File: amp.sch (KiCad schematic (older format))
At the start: 25 parts, among them Q2 MMBF170, Q3 IRF510, Q4 IRF510, T1 8:8, T2 8:8, T3 2:3

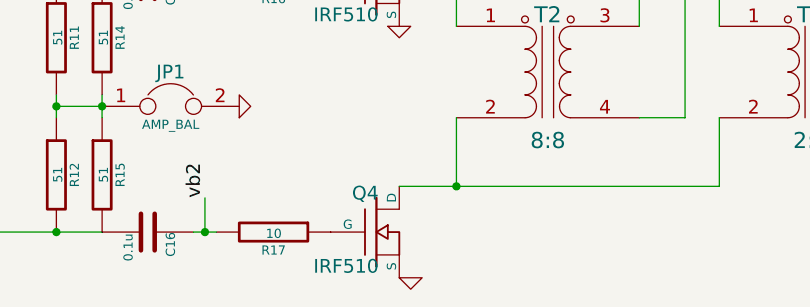
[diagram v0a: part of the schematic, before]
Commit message: All layed out
Several net errors fixed, and some mcu pins reassigned for better layout.
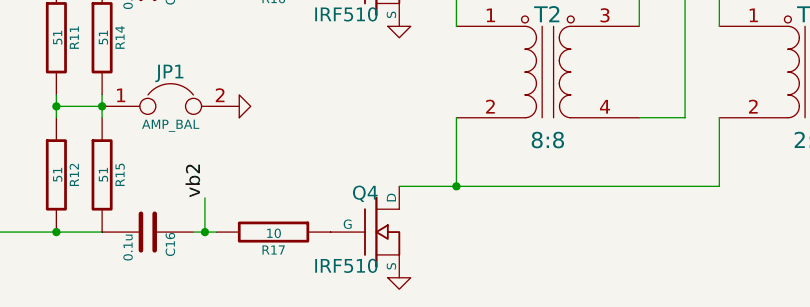
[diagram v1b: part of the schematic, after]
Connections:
- net GND: now also Q4.S
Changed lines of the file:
@@
 L GND #PWR047
 U 1 1 5470F610
-P 7150 5600
-F 0 "#PWR047" H 7150 5600 30  0001 C CNN
-F 1 "GND" H 7150 5530 30  0001 C CNN
-F 2 "" H 7150 5600 60  0000 C CNN
-F 3 "" H 7150 5600 60  0000 C CNN
-	1    7150 5600
+P 7100 5600
+F 0 "#PWR047" H 7100 5600 30  0001 C CNN
+F 1 "GND" H 7100 5530 30  0001 C CNN
+F 2 "" H 7100 5600 60  0000 C CNN
+F 3 "" H 7100 5600 60  0000 C CNN
+	1    7100 5600
 	1    0    0    -1
 $EndComp

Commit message: Schematic changes to go with #3 (extending sot23 pads)
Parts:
- Q2: footprint nu9j-footprints:sot23-DGS -> nu9j-footprints:SOT-23-DGS_HandSoldering
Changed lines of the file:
@@
 F 0 "Q2" H 4660 3670 60  0000 R CNN
 F 1 "MMBF170" H 4660 3350 60  0000 R CNN
-F 2 "nu9j-footprints:sot23-DGS" H 4650 3500 60  0001 C CNN
+F 2 "nu9j-footprints:SOT-23-DGS_HandSoldering" H 4650 3500 60  0001 C CNN
 F 3 "" H 4650 3500 60  0000 C CNN
 	1    4650 3500

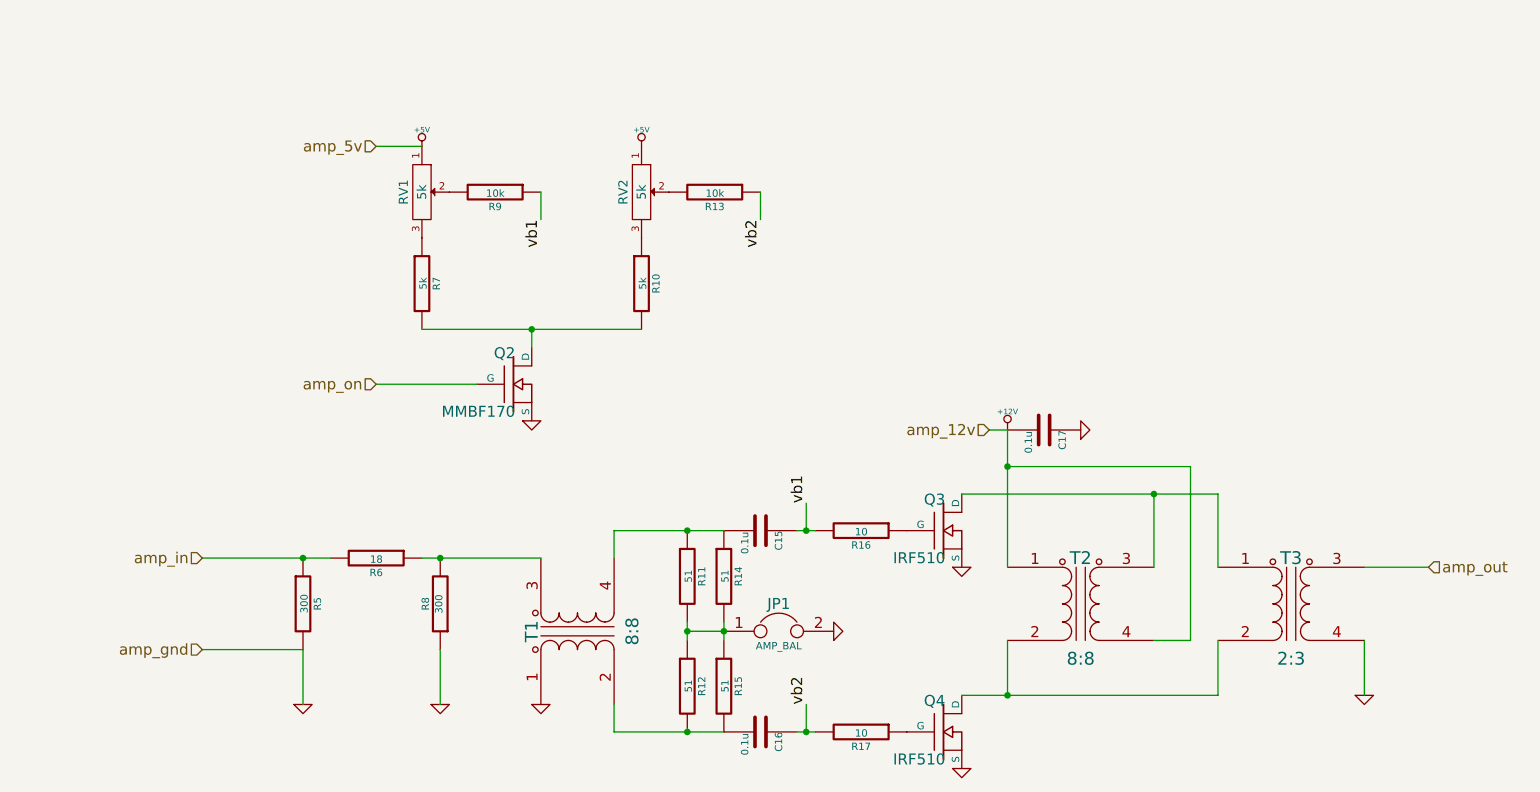
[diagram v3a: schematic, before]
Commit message: Fixes #9: gate bias broken
Replaces Q2 with LTV-356T opto-coupler between 5V and bias rail
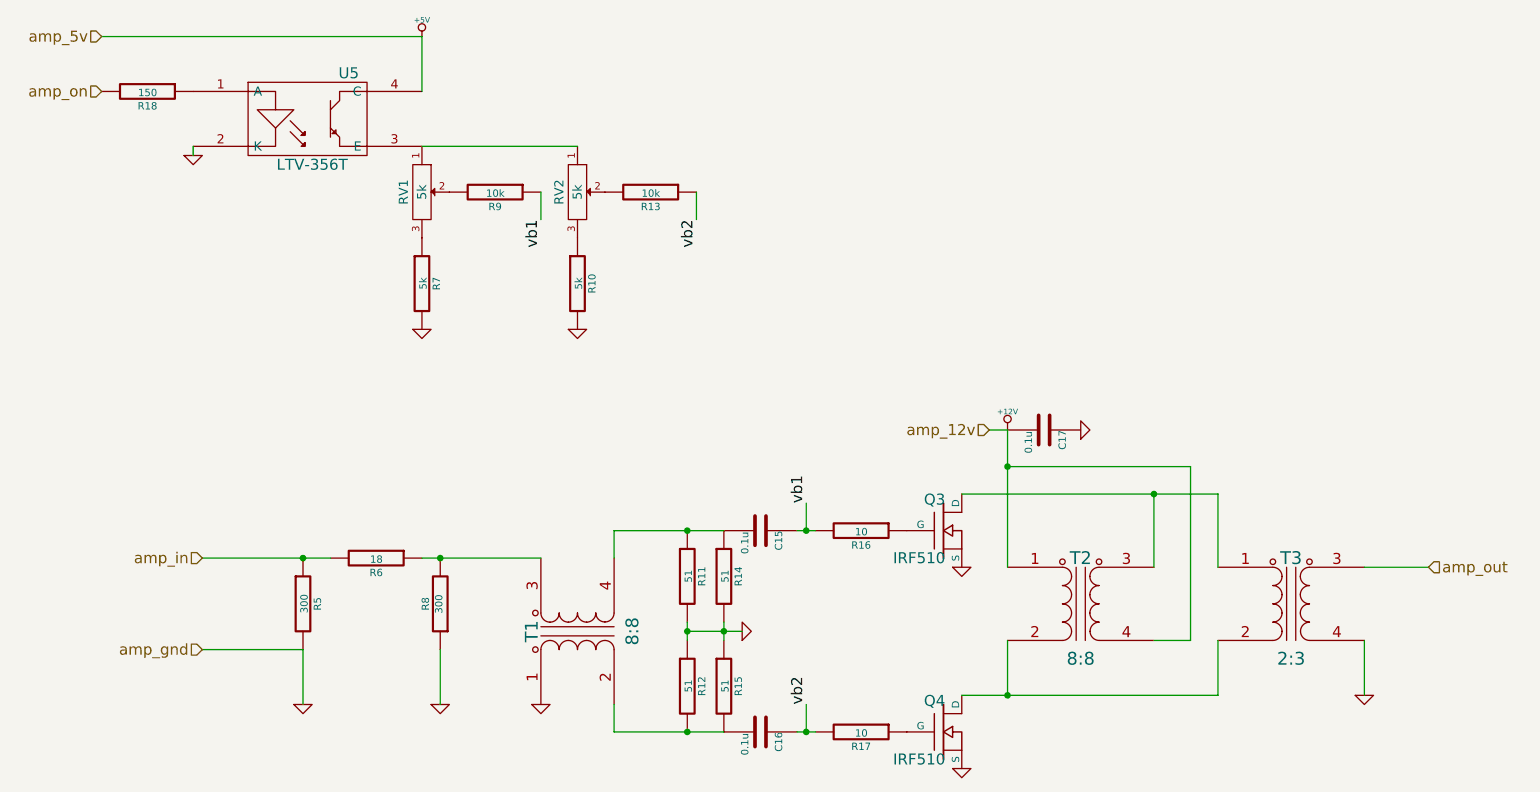
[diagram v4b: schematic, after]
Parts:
- removed JP1: AMP_BAL, Pin_Headers:Pin_Header_Straight_1x02, symbol JUMPER
- removed Q2: MMBF170, nu9j-footprints:SOT-23-DGS_HandSoldering, symbol MOSFET_N
- added R18: 150, Resistors_SMD:R_1206_HandSoldering, symbol R
- added U5: LTV-356T, Opto-Devices:Optocoupler_SMD_HandSoldering_KPC357_LTV35x_PC357_SingleChannel, symbol OPTO-TRANSISTOR4
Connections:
- net +5V: now also U5.4 (C); no longer RV1.1, RV2.1
- net GND: now also R10.2, R11.2, R12.1, R14.2, R15.1, R7.2, U5.2 (K)
- net amp_on: now also R18.2
- new net: RV1.1, RV2.1, U5.3 (E)
- new net: R18.1, U5.1 (A)
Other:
- moved on the sheet: R10, R13, RV2
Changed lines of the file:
@@
 L POT RV2
 U 1 1 5470F7B3
-P 5350 2450
-F 0 "RV2" H 5350 2350 50  0000 C CNN
-F 1 "5k" H 5350 2450 50  0000 C CNN
-F 2 "nu9j-footprints:Potentiometer_Trimmer_Piher_PT10_H01" H 5350 2450 60  0001 C CNN
-F 3 "" H 5350 2450 60  0000 C CNN
-	1    5350 2450
+P 5000 2450
+F 0 "RV2" H 5000 2350 50  0000 C CNN
+F 1 "5k" H 5000 2450 50  0000 C CNN
+F 2 "nu9j-footprints:Potentiometer_Trimmer_Piher_PT10_H01" H 5000 2450 60  0001 C CNN
+F 3 "" H 5000 2450 60  0000 C CNN
+	1    5000 2450
 	0    1    1    0
 $EndComp
@@
 L R R10
 U 1 1 5470F7D4
-P 5350 2950
-F 0 "R10" V 5430 2950 40  0000 C CNN
-F 1 "5k" V 5357 2951 40  0000 C CNN
-F 2 "Resistors_SMD:R_1206_HandSoldering" V 5280 2950 30  0001 C CNN
-F 3 "" H 5350 2950 30  0000 C CNN
-	1    5350 2950
+P 5000 2950
+F 0 "R10" V 5080 2950 40  0000 C CNN
+F 1 "5k" V 5007 2951 40  0000 C CNN
+F 2 "Resistors_SMD:R_1206_HandSoldering" V 4930 2950 30  0001 C CNN
+F 3 "" H 5000 2950 30  0000 C CNN
+	1    5000 2950
 	1    0    0    -1
 $EndComp
@@
 L R R13
 U 1 1 5470F80E
-P 5750 2450
-F 0 "R13" V 5830 2450 40  0000 C CNN
-F 1 "10k" V 5757 2451 40  0000 C CNN
-F 2 "Resistors_SMD:R_1206_HandSoldering" V 5680 2450 30  0001 C CNN
-F 3 "" H 5750 2450 30  0000 C CNN
-	1    5750 2450
+P 5400 2450
+F 0 "R13" V 5480 2450 40  0000 C CNN
+F 1 "10k" V 5407 2451 40  0000 C CNN
+F 2 "Resistors_SMD:R_1206_HandSoldering" V 5330 2450 30  0001 C CNN
+F 3 "" H 5400 2450 30  0000 C CNN
+	1    5400 2450
 	0    1    1    0
 $EndComp
@@
 L +5V #PWR049
 U 1 1 5470F81B
-P 4150 2200
-F 0 "#PWR049" H 4150 2290 20  0001 C CNN
-F 1 "+5V" H 4150 2290 30  0000 C CNN
-F 2 "" H 4150 2200 60  0000 C CNN
-F 3 "" H 4150 2200 60  0000 C CNN
-	1    4150 2200
+P 4150 1600
+F 0 "#PWR049" H 4150 1690 20  0001 C CNN
+F 1 "+5V" H 4150 1690 30  0000 C CNN
+F 2 "" H 4150 1600 60  0000 C CNN
+F 3 "" H 4150 1600 60  0000 C CNN
+	1    4150 1600
 	1    0    0    -1
 $EndComp
@@
 L GND #PWR050
 U 1 1 5470F84C
-P 4750 3700
-F 0 "#PWR050" H 4750 3700 30  0001 C CNN
-F 1 "GND" H 4750 3630 30  0001 C CNN
-F 2 "" H 4750 3700 60  0000 C CNN
-F 3 "" H 4750 3700 60  0000 C CNN
-	1    4750 3700
+P 2900 2250
+F 0 "#PWR050" H 2900 2250 30  0001 C CNN
+F 1 "GND" H 2900 2180 30  0001 C CNN
+F 2 "" H 2900 2250 60  0000 C CNN
+F 3 "" H 2900 2250 60  0000 C CNN
+	1    2900 2250
 	1    0    0    -1
 $EndComp
@@
 vb1
 Wire Wire Line
-	6000 2450 6000 2600
-Text Label 6000 2600 3    60   ~ 0
+	5650 2450 5650 2600
+Text Label 5650 2600 3    60   ~ 0
 vb2
 Wire Wire Line
@@
 L GND #PWR053
 U 1 1 5470FB98
-P 6400 4850
-F 0 "#PWR053" H 6400 4850 30  0001 C CNN
-F 1 "GND" H 6400 4780 30  0001 C CNN
-F 2 "" H 6400 4850 60  0000 C CNN
-F 3 "" H 6400 4850 60  0000 C CNN
-	1    6400 4850
+P 5900 4850
+F 0 "#PWR053" H 5900 4850 30  0001 C CNN
+F 1 "GND" H 5900 4780 30  0001 C CNN
+F 2 "" H 5900 4850 60  0000 C CNN
+F 3 "" H 5900 4850 60  0000 C CNN
+	1    5900 4850
 	0    -1   -1   0
 $EndComp
 Wire Wire Line
-	5600 4850 5800 4850
+	5600 4850 5900 4850
 Connection ~ 5800 4850
 Connection ~ 5600 4850
-$Comp
-L JUMPER JP1
-U 1 1 5470FBEE
-P 6100 4850
-F 0 "JP1" H 6100 5000 60  0000 C CNN
-F 1 "AMP_BAL" H 6100 4770 40  0000 C CNN
-F 2 "Pin_Headers:Pin_Header_Straight_1x02" H 6100 4850 60  0001 C CNN
-F 3 "" H 6100 4850 60  0000 C CNN
-	1    6100 4850
-	1    0    0    -1
-$EndComp
-$Comp
-L MOSFET_N Q2
-U 1 1 5470FC2F
-P 4650 3500
-F 0 "Q2" H 4660 3670 60  0000 R CNN
-F 1 "MMBF170" H 4660 3350 60  0000 R CNN
-F 2 "nu9j-footprints:SOT-23-DGS_HandSoldering" H 4650 3500 60  0001 C CNN
-F 3 "" H 4650 3500 60  0000 C CNN
-	1    4650 3500
-	1    0    0    -1
-$EndComp
-Wire Wire Line
-	4150 3200 5350 3200
-Wire Wire Line
-	4750 3200 4750 3300
-Connection ~ 4750 3200
-$Comp
-L +5V #PWR054
-U 1 1 5470FCA2
-P 5350 2200
-F 0 "#PWR054" H 5350 2290 20  0001 C CNN
-F 1 "+5V" H 5350 2290 30  0000 C CNN
-F 2 "" H 5350 2200 60  0000 C CNN
-F 3 "" H 5350 2200 60  0000 C CNN
-	1    5350 2200
-	1    0    0    -1
-$EndComp
-Wire Wire Line
-	4450 3500 3900 3500
-Text HLabel 3900 3500 0    60   Input ~ 0
+Text HLabel 2400 1900 0    60   Input ~ 0
 amp_on
 Wire Wire Line
@@
 Wire Wire Line
 	7350 3750 7250 3750
-Wire Wire Line
-	4150 2200 3900 2200
-Text HLabel 3900 2200 0    60   Input ~ 0
+Text HLabel 2400 1600 0    60   Input ~ 0
 amp_5v
 Text HLabel 7250 3750 0    60   Input ~ 0
 amp_12v
+$Comp
+L OPTO-TRANSISTOR4 U5
+U 1 1 5596F157
+P 3550 2050
+F 0 "U5" H 3750 2300 60  0000 C CNN
+F 1 "LTV-356T" H 3550 1800 60  0000 C CNN
+F 2 "Opto-Devices:Optocoupler_SMD_HandSoldering_KPC357_LTV35x_PC357_SingleChannel" H 3550 2050 60  0001 C CNN
+F 3 "" H 3550 2050 60  0000 C CNN
+	1    3550 2050
+	1    0    0    -1
+$EndComp
+Wire Wire Line
+	2900 2200 2900 2250
+Wire Wire Line
+	4150 1900 4150 1600
+$Comp
+L GND #PWR055
+U 1 1 5596F601
+P 4150 3200
+F 0 "#PWR055" H 4150 3200 30  0001 C CNN
+F 1 "GND" H 4150 3130 30  0001 C CNN
+F 2 "" H 4150 3200 60  0000 C CNN
+F 3 "" H 4150 3200 60  0000 C CNN
+	1    4150 3200
+	1    0    0    -1
+$EndComp
+$Comp
+L GND #PWR056
+U 1 1 5596F624
+P 5000 3200
+F 0 "#PWR056" H 5000 3200 30  0001 C CNN
+F 1 "GND" H 5000 3130 30  0001 C CNN
+F 2 "" H 5000 3200 60  0000 C CNN
+F 3 "" H 5000 3200 60  0000 C CNN
+	1    5000 3200
+	1    0    0    -1
+$EndComp
+$Comp
+L R R18
+U 1 1 55970003
+P 2650 1900
+F 0 "R18" V 2730 1900 40  0000 C CNN
+F 1 "150" V 2657 1901 40  0000 C CNN
+F 2 "Resistors_SMD:R_1206_HandSoldering" V 2580 1900 30  0001 C CNN
+F 3 "" H 2650 1900 30  0000 C CNN
+	1    2650 1900
+	0    1    1    0
+$EndComp
+Wire Wire Line
+	4150 1600 2400 1600
+Wire Wire Line
+	4150 2200 5000 2200
 $EndSCHEMATC

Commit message: Fixes #8: transistor placement
Also, this is a major board layout change

- Added more 12V filtering caps
- Placed fuse in front of filtering caps
- Changed IRF510 footprints to horizontal lower side w/ mounting hole
- Expanded layout to fill new board size
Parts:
- Q3, Q4: footprint Transistors_TO-220:TO-220_FET-GDS_Vertical_LargePads -> Transistors_TO-220:TO-220_FET-GDS_Horizontal_MountedFromLS_LargePads
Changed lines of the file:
@@
 F 0 "Q3" H 7010 4470 60  0000 R CNN
 F 1 "IRF510" H 7010 4150 60  0000 R CNN
-F 2 "Transistors_TO-220:TO-220_FET-GDS_Vertical_LargePads" H 7000 4300 60  0001 C CNN
+F 2 "Transistors_TO-220:TO-220_FET-GDS_Horizontal_MountedFromLS_LargePads" H 7000 4300 60  0001 C CNN
 F 3 "" H 7000 4300 60  0000 C CNN
 	1    7000 4300
@@
 F 0 "Q4" H 7010 5570 60  0000 R CNN
 F 1 "IRF510" H 7010 5250 60  0000 R CNN
-F 2 "Transistors_TO-220:TO-220_FET-GDS_Vertical_LargePads" H 7000 5400 60  0001 C CNN
+F 2 "Transistors_TO-220:TO-220_FET-GDS_Horizontal_MountedFromLS_LargePads" H 7000 5400 60  0001 C CNN
 F 3 "" H 7000 5400 60  0000 C CNN
 	1    7000 5400
@@
 	2950 4450 3650 4450
 $Comp
-L GND #PWR043
+L GND #PWR048
 U 1 1 5470F4C6
 P 4800 5250
-F 0 "#PWR043" H 4800 5250 30  0001 C CNN
+F 0 "#PWR048" H 4800 5250 30  0001 C CNN
 F 1 "GND" H 4800 5180 30  0001 C CNN
 F 2 "" H 4800 5250 60  0000 C CNN
@@
 $EndComp
 $Comp
-L GND #PWR044
+L GND #PWR049
 U 1 1 5470F4DA
 P 4250 5250
-F 0 "#PWR044" H 4250 5250 30  0001 C CNN
+F 0 "#PWR049" H 4250 5250 30  0001 C CNN
 F 1 "GND" H 4250 5180 30  0001 C CNN
 F 2 "" H 4250 5250 60  0000 C CNN
@@
 $EndComp
 $Comp
-L GND #PWR045
+L GND #PWR050
 U 1 1 5470F4EE
 P 3500 5250
-F 0 "#PWR045" H 3500 5250 30  0001 C CNN
+F 0 "#PWR050" H 3500 5250 30  0001 C CNN
 F 1 "GND" H 3500 5180 30  0001 C CNN
 F 2 "" H 3500 5250 60  0000 C CNN
@@
 Connection ~ 7350 3950
 $Comp
-L GND #PWR046
+L GND #PWR051
 U 1 1 5470F5FC
 P 7100 4500
-F 0 "#PWR046" H 7100 4500 30  0001 C CNN
+F 0 "#PWR051" H 7100 4500 30  0001 C CNN
 F 1 "GND" H 7100 4430 30  0001 C CNN
 F 2 "" H 7100 4500 60  0000 C CNN
@@
 $EndComp
 $Comp
-L GND #PWR047
+L GND #PWR052
 U 1 1 5470F610
 P 7100 5600
-F 0 "#PWR047" H 7100 5600 30  0001 C CNN
+F 0 "#PWR052" H 7100 5600 30  0001 C CNN
 F 1 "GND" H 7100 5530 30  0001 C CNN
 F 2 "" H 7100 5600 60  0000 C CNN
@@
 amp_in
 $Comp
-L GND #PWR048
+L GND #PWR053
 U 1 1 5470F625
 P 9300 5200
-F 0 "#PWR048" H 9300 5200 30  0001 C CNN
+F 0 "#PWR053" H 9300 5200 30  0001 C CNN
 F 1 "GND" H 9300 5130 30  0001 C CNN
 F 2 "" H 9300 5200 60  0000 C CNN
@@
 $EndComp
 $Comp
-L +5V #PWR049
+L +5V #PWR054
 U 1 1 5470F81B
 P 4150 1600
-F 0 "#PWR049" H 4150 1690 20  0001 C CNN
+F 0 "#PWR054" H 4150 1690 20  0001 C CNN
 F 1 "+5V" H 4150 1690 30  0000 C CNN
 F 2 "" H 4150 1600 60  0000 C CNN
@@
 $EndComp
 $Comp
-L GND #PWR050
+L GND #PWR055
 U 1 1 5470F84C
 P 2900 2250
-F 0 "#PWR050" H 2900 2250 30  0001 C CNN
+F 0 "#PWR055" H 2900 2250 30  0001 C CNN
 F 1 "GND" H 2900 2180 30  0001 C CNN
 F 2 "" H 2900 2250 60  0000 C CNN
@@
 vb2
 $Comp
-L +12V #PWR051
+L +12V #PWR056
 U 1 1 5470F9E0
 P 7350 3750
-F 0 "#PWR051" H 7350 3700 20  0001 C CNN
+F 0 "#PWR056" H 7350 3700 20  0001 C CNN
 F 1 "+12V" H 7350 3850 30  0000 C CNN
 F 2 "" H 7350 3750 60  0000 C CNN
@@
 $EndComp
 $Comp
-L GND #PWR052
+L GND #PWR057
 U 1 1 5470FA0D
 P 7750 3750
-F 0 "#PWR052" H 7750 3750 30  0001 C CNN
+F 0 "#PWR057" H 7750 3750 30  0001 C CNN
 F 1 "GND" H 7750 3680 30  0001 C CNN
 F 2 "" H 7750 3750 60  0000 C CNN
@@
 $EndComp
 $Comp
-L GND #PWR053
+L GND #PWR058
 U 1 1 5470FB98
 P 5900 4850
-F 0 "#PWR053" H 5900 4850 30  0001 C CNN
+F 0 "#PWR058" H 5900 4850 30  0001 C CNN
 F 1 "GND" H 5900 4780 30  0001 C CNN
 F 2 "" H 5900 4850 60  0000 C CNN
@@
 	4150 1900 4150 1600
 $Comp
-L GND #PWR055
+L GND #PWR059
 U 1 1 5596F601
 P 4150 3200
-F 0 "#PWR055" H 4150 3200 30  0001 C CNN
+F 0 "#PWR059" H 4150 3200 30  0001 C CNN
 F 1 "GND" H 4150 3130 30  0001 C CNN
 F 2 "" H 4150 3200 60  0000 C CNN
@@
 $EndComp
 $Comp
-L GND #PWR056
+L GND #PWR060
 U 1 1 5596F624
 P 5000 3200
-F 0 "#PWR056" H 5000 3200 30  0001 C CNN
+F 0 "#PWR060" H 5000 3200 30  0001 C CNN
 F 1 "GND" H 5000 3130 30  0001 C CNN
 F 2 "" H 5000 3200 60  0000 C CNN
